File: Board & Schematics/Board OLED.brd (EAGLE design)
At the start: 25.4 x 25.4 mm, 23 parts

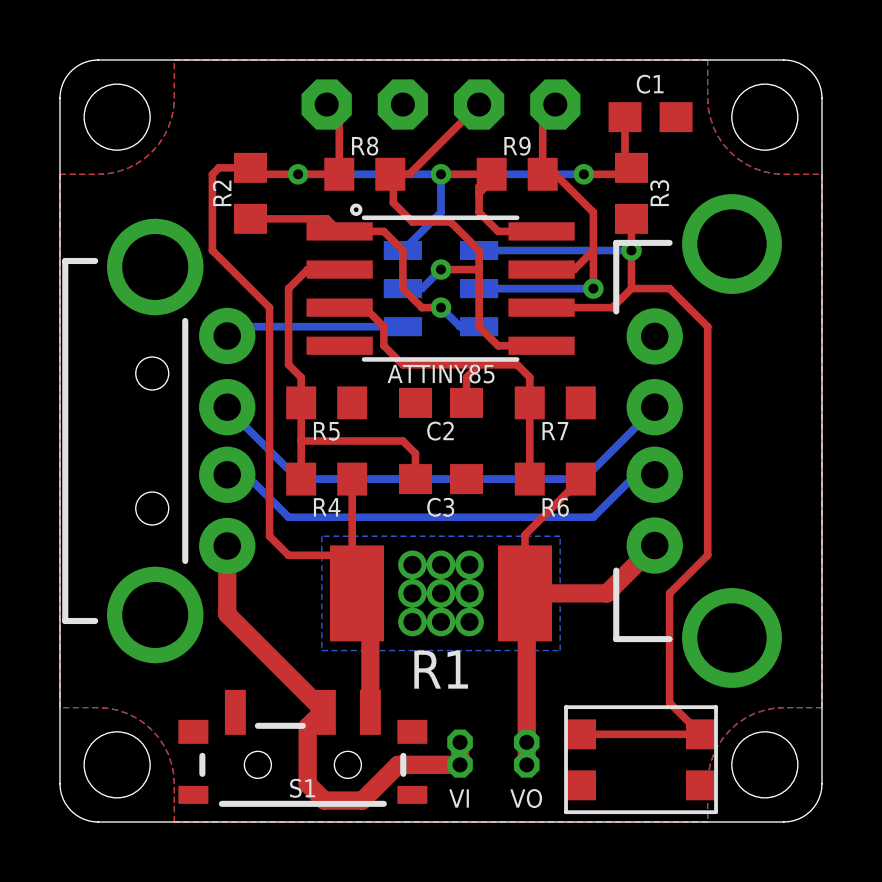
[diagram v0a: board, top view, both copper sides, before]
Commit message: removed cream from bottom ICSP Header
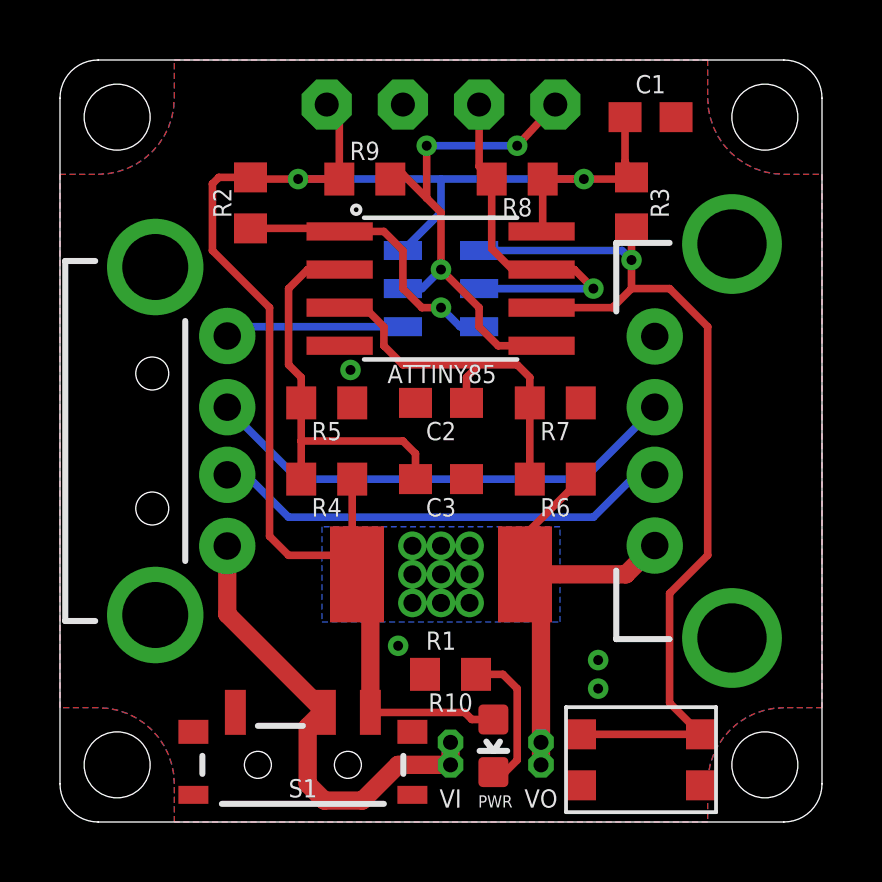
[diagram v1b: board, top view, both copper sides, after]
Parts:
- added PWR: (no value), SparkFun-LED:LED-0603
- added R10: 91Ω, rcl:R0603
- U$3: device OwnStuff:LOGO-SILKSCREEN -> OwnStuff:LOGO-SILKSCREEEN-S
- U$4: device SparkFun-Aesthetics:OSHW-LOGO-M -> SparkFun-Aesthetics:OSHW-LOGO-S
- moved U$4 14.3 mm to (9.05, 12.9)
- moved R8 5.08 mm to (15.2, 21.4), turned to 0 degrees
- moved R9 5.08 mm to (10.2, 21.4)
- moved U$3 2.34 mm to (14.9, 12.5)
- moved R1 0.64 mm to (12.7, 8.26)
- moved VO 0.48 mm to (16.0, 1.91)
- moved VI 0.32 mm to (13.0, 1.91)
- moved R2 0.32 mm to (6.35, 20.6)
- moved R3 0.32 mm to (19.1, 20.6)
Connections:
- new net N$4: PWR.C, R10.2
- net +5V: now also PWR.A
- net GND: now also R10.1
- net MOSI: now also R9.1, U$2.SDA; no longer R8.1, U$2.SCL
- net SCK: now also R8.1, U$2.SCL; no longer R9.1, U$2.SDA
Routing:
- net N$4: track 0.00 -> 4.91 mm
- net +5V: track 53.9 -> 56.7 mm, vias 3 -> 2
- net MOSI: track 16.1 -> 17.1 mm, vias 1 -> 3
- net N$6: track 15.8 -> 16.6 mm
- net GND: vias 0 -> 4

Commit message: added soldermask from vias
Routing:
- net GND: vias 4 -> 5

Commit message: fixed silkscreen and schematic designator for new, smaller shunt
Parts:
- R1: value 1Ω -> 0.1Ω
- moved R3 0.32 mm to (19.1, 21.0)
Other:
- board text added: "Shunt: 0.1Ω VI-VO=I[A]/10"
- board text removed: "Shunt: 1Ω VI-VO=I[A]"

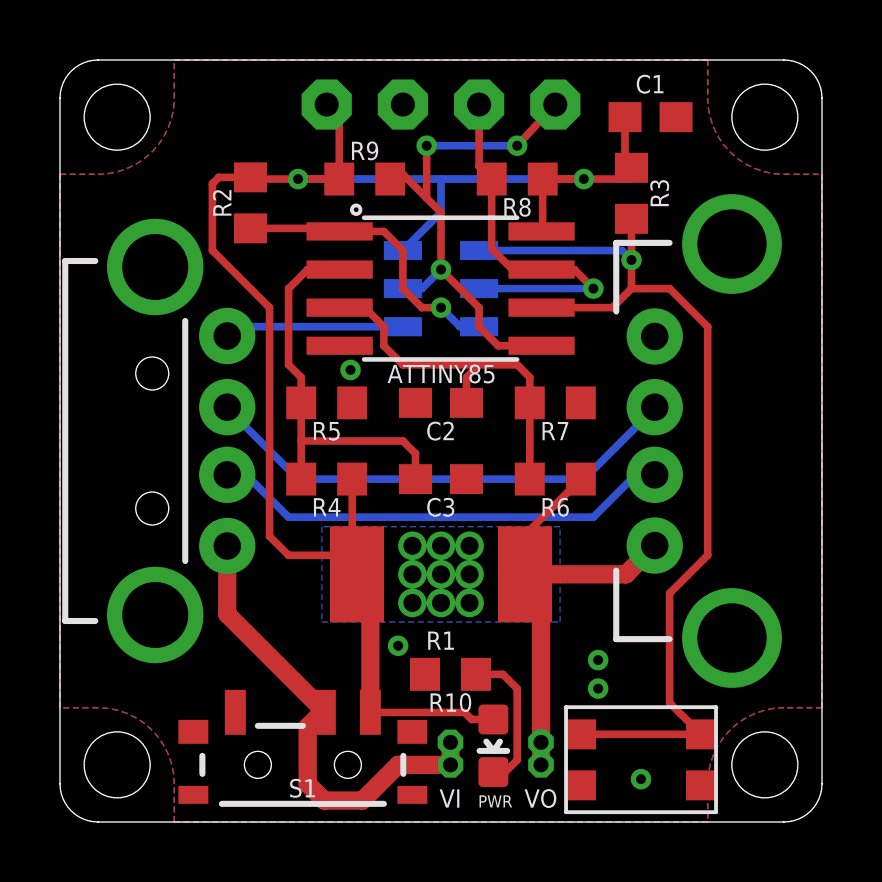
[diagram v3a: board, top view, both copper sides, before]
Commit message: remove attenuation from OLED variant
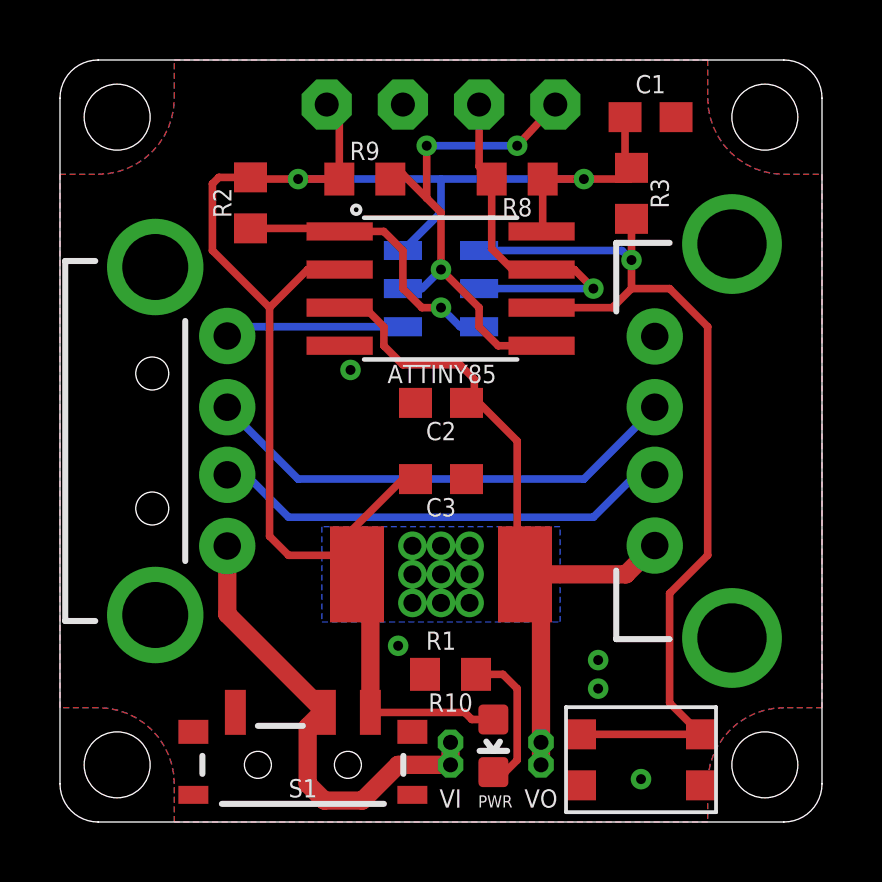
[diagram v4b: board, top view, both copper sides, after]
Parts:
- removed R4, R6: 10kΩ, rcl:R0603
- removed R5, R7: 2kΩ, rcl:R0603
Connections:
- removed net N$6: OUTPUT.VBUS, R1.2, R6.2, VO.P$1, VO.P$2
- removed net VSENSE: ATTINY85.2, C3.1, R4.1, R5.2
- net +5V: now also ATTINY85.2, C3.1; no longer R4.2
- net GND: no longer R5.1, R7.1
- net ISENSE: now also OUTPUT.VBUS, R1.2, VO.P$1, VO.P$2; no longer R6.1, R7.2
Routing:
- net N$6: track 16.6 -> 0.00 mm
- net ISENSE: track 12.5 -> 26.2 mm
- net VSENSE: track 13.3 -> 0.00 mm
- net +5V: track 56.7 -> 60.4 mm
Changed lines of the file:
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@@
 </element>
 <element name="U$1" library="OwnStuff" package="ICSP-SMD" value="ICSPSMD" x="12.7" y="17.78" rot="MR0"/>
-<element name="R4" library="rcl" package="R0603" value="10kΩ" x="8.89" y="11.43" smashed="yes">
-<attribute name="NAME" x="8.89" y="10.795" size="0.6096" layer="25" align="top-center"/>
-<attribute name="VALUE" x="8.255" y="9.525" size="1.27" layer="27"/>
-</element>
-<element name="R5" library="rcl" package="R0603" value="2kΩ" x="8.89" y="13.97" smashed="yes" rot="R180">
-<attribute name="NAME" x="8.89" y="13.335" size="0.6096" layer="25" rot="R180" align="bottom-center"/>
-<attribute name="VALUE" x="9.525" y="15.875" size="1.27" layer="27" rot="R180"/>
-</element>
-<element name="R6" library="rcl" package="R0603" value="10kΩ" x="16.51" y="11.43" smashed="yes">
-<attribute name="NAME" x="16.51" y="10.795" size="0.6096" layer="25" align="top-center"/>
-<attribute name="VALUE" x="15.875" y="9.525" size="1.27" layer="27"/>
-</element>
-<element name="R7" library="rcl" package="R0603" value="2kΩ" x="16.51" y="13.97" smashed="yes" rot="R180">
-<attribute name="NAME" x="16.51" y="13.335" size="0.6096" layer="25" rot="R180" align="bottom-center"/>
-<attribute name="VALUE" x="17.145" y="15.875" size="1.27" layer="27" rot="R180"/>
-</element>
 <element name="S1" library="SparkFun-Electromechanical" package="SWITCH-SPST-SMD-A" value="" x="8.09625" y="1.905" smashed="yes" rot="R180">
 <attribute name="NAME" x="8.09625" y="1.42875" size="0.6096" layer="25" rot="R180" align="bottom-center"/>
@@
 <contactref element="U$2" pad="GND"/>
 <contactref element="U$1" pad="GND"/>
-<contactref element="R5" pad="1"/>
-<contactref element="R7" pad="1"/>
 <contactref element="C2" pad="2"/>
 <contactref element="C3" pad="2"/>
@@
 <contactref element="S1" pad="1"/>
 <contactref element="R1" pad="1"/>
-<contactref element="R4" pad="2"/>
 <wire x1="9.87" y1="7.59" x2="9.9" y2="8.255" width="0.4064" layer="1"/>
-<wire x1="9.9" y1="11.27" x2="9.74" y2="11.43" width="0.254" layer="1"/>
-<wire x1="9.74" y1="11.43" x2="9.74" y2="8.89" width="0.254" layer="1"/>
 <wire x1="9.74" y1="8.89" x2="9.74" y2="7.78" width="0.254" layer="1"/>
 <wire x1="9.74" y1="7.78" x2="9.9" y2="8.255" width="0.254" layer="1"/>
@@
 <wire x1="13.49375" y1="3.65125" x2="10.35" y2="3.65125" width="0.254" layer="1"/>
 <wire x1="10.35" y1="3.65125" x2="10.34625" y2="3.655" width="0.254" layer="1"/>
+<contactref element="C3" pad="1"/>
+<wire x1="9.74" y1="8.89" x2="9.74" y2="9.74" width="0.254" layer="1"/>
+<wire x1="9.74" y1="9.74" x2="11.43" y2="11.43" width="0.254" layer="1"/>
+<wire x1="11.43" y1="11.43" x2="11.85" y2="11.43" width="0.254" layer="1"/>
+<contactref element="ATTINY85" pad="2"/>
+<wire x1="9.3218" y1="18.415" x2="8.255" y2="18.415" width="0.254" layer="1"/>
+<wire x1="8.255" y1="18.415" x2="6.985" y2="17.145" width="0.254" layer="1"/>
 </signal>
 <signal name="RST">
@@
 <wire x1="11.43" y1="19.05" x2="10.795" y2="19.685" width="0.254" layer="1"/>
 <wire x1="10.795" y1="19.685" x2="9.3218" y2="19.685" width="0.254" layer="1"/>
-</signal>
-<signal name="N$6">
-<contactref element="R1" pad="2"/>
-<contactref element="OUTPUT" pad="VBUS"/>
-<contactref element="R6" pad="2"/>
-<wire x1="15.5" y1="8.255" x2="15.5" y2="9.57" width="0.254" layer="1"/>
-<wire x1="15.5" y1="9.57" x2="17.36" y2="11.43" width="0.254" layer="1"/>
-<contactref element="VO" pad="P$2"/>
-<contactref element="VO" pad="P$1"/>
-<wire x1="15.5" y1="8.255" x2="18.865" y2="8.255" width="0.6096" layer="1"/>
-<wire x1="15.24" y1="7.36" x2="15.5" y2="8.255" width="0.6096" layer="1"/>
-<wire x1="15.5575" y1="7.6775" x2="15.5" y2="8.255" width="0.6096" layer="1"/>
-<wire x1="16.03375" y1="1.905" x2="16.03375" y2="2.655" width="0.6096" layer="1"/>
-<wire x1="16.03375" y1="2.655" x2="16.03375" y2="7.08625" width="0.6096" layer="1"/>
-<wire x1="16.03375" y1="7.08625" x2="15.5" y2="8.255" width="0.6096" layer="1"/>
-<wire x1="18.865" y1="8.255" x2="19.825" y2="9.215" width="0.6096" layer="1"/>
 </signal>
 <signal name="MOSI">
@@
 <wire x1="18.415" y1="17.145" x2="19.05" y2="17.78" width="0.254" layer="1"/>
 </signal>
-<signal name="VSENSE">
-<contactref element="ATTINY85" pad="2"/>
-<contactref element="R4" pad="1"/>
-<contactref element="R5" pad="2"/>
-<contactref element="C3" pad="1"/>
-<wire x1="8.04" y1="13.97" x2="8.04" y2="14.82" width="0.254" layer="1"/>
-<wire x1="8.04" y1="14.82" x2="7.62" y2="15.24" width="0.254" layer="1"/>
-<wire x1="7.62" y1="15.24" x2="7.62" y2="17.78" width="0.254" layer="1"/>
-<wire x1="7.62" y1="17.78" x2="8.255" y2="18.415" width="0.254" layer="1"/>
-<wire x1="8.255" y1="18.415" x2="9.3218" y2="18.415" width="0.254" layer="1"/>
-<wire x1="8.04" y1="11.43" x2="8.04" y2="12.7" width="0.254" layer="1"/>
-<wire x1="8.04" y1="12.7" x2="8.04" y2="13.97" width="0.254" layer="1"/>
-<wire x1="11.85" y1="11.43" x2="11.85" y2="12.28" width="0.254" layer="1"/>
-<wire x1="11.85" y1="12.28" x2="11.43" y2="12.7" width="0.254" layer="1"/>
-<wire x1="11.43" y1="12.7" x2="8.04" y2="12.7" width="0.254" layer="1"/>
-</signal>
 <signal name="ISENSE">
-<contactref element="R6" pad="1"/>
-<contactref element="R7" pad="2"/>
 <contactref element="C2" pad="1"/>
 <contactref element="ATTINY85" pad="3"/>
 <wire x1="10.795" y1="16.51" x2="10.16" y2="17.145" width="0.254" layer="1"/>
 <wire x1="10.16" y1="17.145" x2="9.3218" y2="17.145" width="0.254" layer="1"/>
-<wire x1="15.66" y1="11.43" x2="15.66" y2="13.97" width="0.254" layer="1"/>
-<wire x1="15.66" y1="13.97" x2="15.66" y2="14.82" width="0.254" layer="1"/>
-<wire x1="15.66" y1="14.82" x2="15.24" y2="15.24" width="0.254" layer="1"/>
 <wire x1="10.795" y1="16.51" x2="10.795" y2="15.875" width="0.254" layer="1"/>
 <wire x1="10.795" y1="15.875" x2="11.43" y2="15.24" width="0.254" layer="1"/>
-<wire x1="11.43" y1="15.24" x2="13.97" y2="15.24" width="0.254" layer="1"/>
-<wire x1="13.97" y1="15.24" x2="15.24" y2="15.24" width="0.254" layer="1"/>
-<wire x1="13.55" y1="13.97" x2="13.55" y2="14.82" width="0.254" layer="1"/>
-<wire x1="13.55" y1="14.82" x2="13.97" y2="15.24" width="0.254" layer="1"/>
+<contactref element="R1" pad="2"/>
+<contactref element="OUTPUT" pad="VBUS"/>
+<contactref element="VO" pad="P$2"/>
+<contactref element="VO" pad="P$1"/>
+<wire x1="15.5" y1="8.255" x2="18.865" y2="8.255" width="0.6096" layer="1"/>
+<wire x1="15.24" y1="7.36" x2="15.5" y2="8.255" width="0.6096" layer="1"/>
+<wire x1="15.5575" y1="7.6775" x2="15.5" y2="8.255" width="0.6096" layer="1"/>
+<wire x1="16.03375" y1="1.905" x2="16.03375" y2="2.655" width="0.6096" layer="1"/>
+<wire x1="16.03375" y1="2.655" x2="16.03375" y2="7.08625" width="0.6096" layer="1"/>
+<wire x1="16.03375" y1="7.08625" x2="15.5" y2="8.255" width="0.6096" layer="1"/>
+<wire x1="18.865" y1="8.255" x2="19.825" y2="9.215" width="0.6096" layer="1"/>
+<wire x1="11.43" y1="15.24" x2="13.335" y2="15.24" width="0.254" layer="1"/>
+<wire x1="13.335" y1="15.24" x2="13.81125" y2="14.76375" width="0.254" layer="1"/>
+<wire x1="13.81125" y1="14.76375" x2="13.81125" y2="14.23125" width="0.254" layer="1"/>
+<wire x1="13.81125" y1="14.23125" x2="13.55" y2="13.97" width="0.254" layer="1"/>
+<wire x1="13.55" y1="13.97" x2="13.97" y2="13.97" width="0.254" layer="1"/>
+<wire x1="13.97" y1="13.97" x2="15.24" y2="12.7" width="0.254" layer="1"/>
+<wire x1="15.24" y1="12.7" x2="15.24" y2="8.515" width="0.254" layer="1"/>
+<wire x1="15.24" y1="8.515" x2="15.5" y2="8.255" width="0.254" layer="1"/>
 </signal>
 <signal name="N$3">

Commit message: switched differential measure polarity
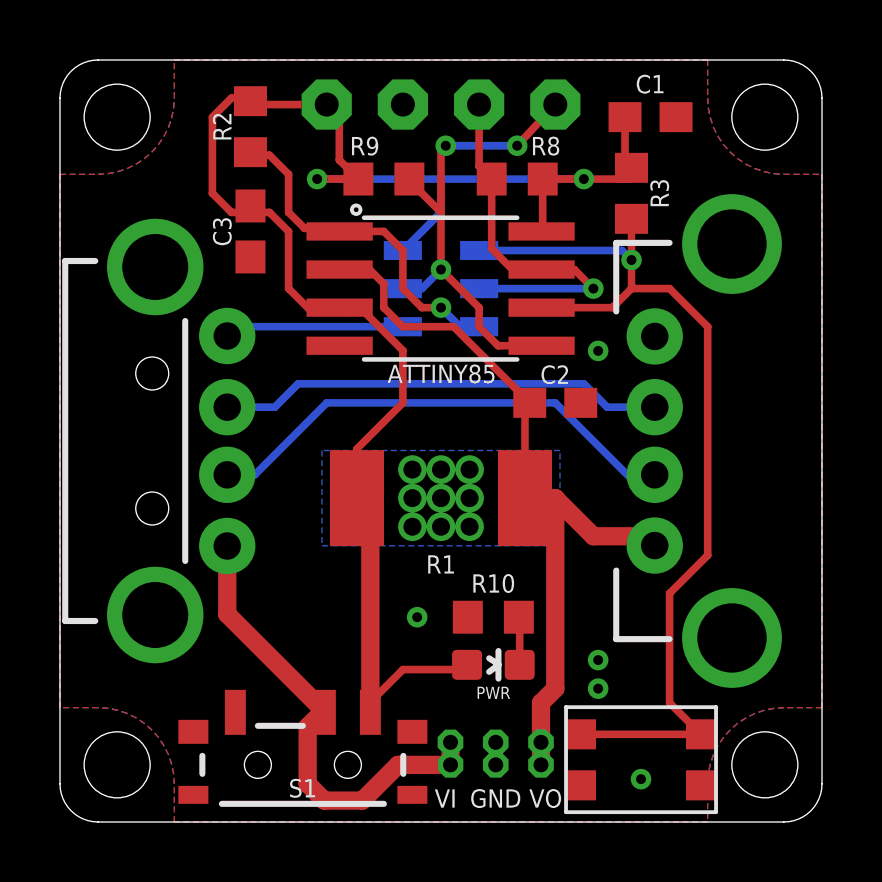
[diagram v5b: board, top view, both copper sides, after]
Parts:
- added GND: TESTPOINT0.5MM-DRILL-WIRE-LOOP, OwnStuff:TP-0.5MM-DUAL
- moved C3 10.4 mm to (6.35, 19.7), turned to 270 degrees
- moved U$4 6.05 mm to (8.57, 6.83)
- moved U$3 5.72 mm to (14.6, 6.83)
- moved C2 3.81 mm to (16.5, 14.0), turned to 0 degrees
- moved PWR 2.70 mm to (14.4, 5.24), turned to 270 degrees
- moved R1 2.54 mm to (12.7, 10.8)
- moved R2 2.54 mm to (6.35, 23.2)
- moved R10 2.38 mm to (14.4, 6.83)
- moved R9 0.63 mm to (10.8, 21.4)
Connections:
- net +5V: now also ATTINY85.3; no longer ATTINY85.2
- net GND: now also GND.P$1, GND.P$2
- net ISENSE: now also ATTINY85.2; no longer ATTINY85.3
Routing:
- net +5V: track 60.4 -> 56.7 mm
- net N$4: track 4.91 -> 1.60 mm
- net RST: track 9.72 -> 11.5 mm
- net N$1: track 16.4 -> 15.0 mm
- net N$2: track 15.4 -> 16.4 mm
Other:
- board text added: "GND"

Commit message: added attenuation resistor network to mode switch pin
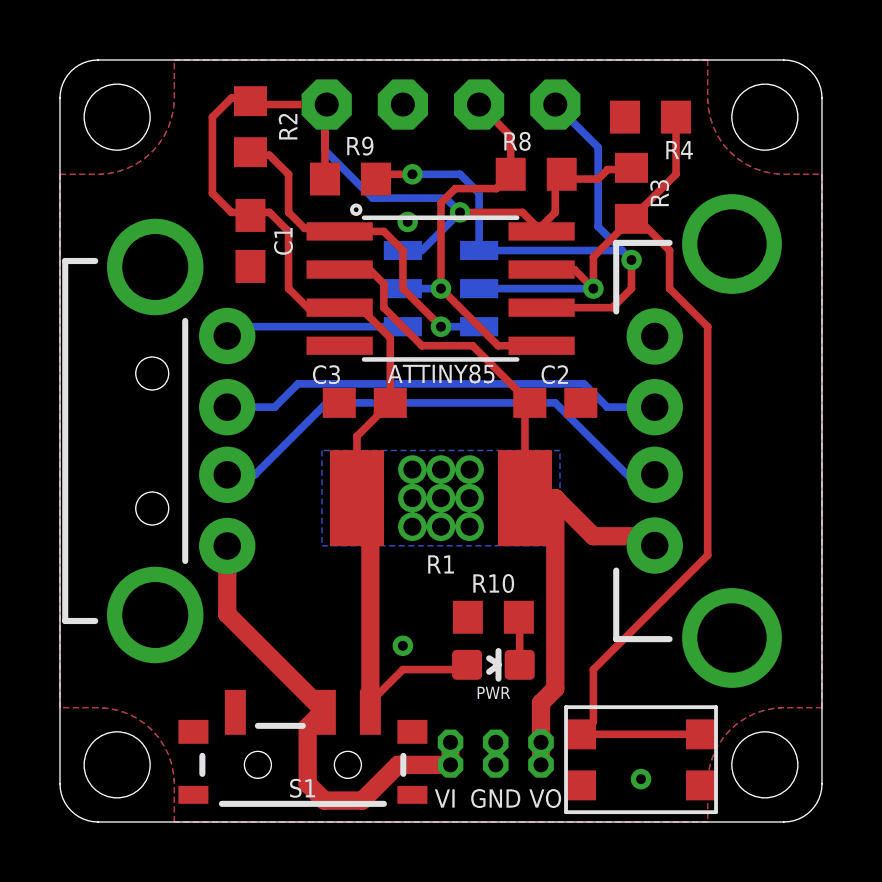
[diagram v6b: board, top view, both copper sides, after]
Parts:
- added R4: 2kΩ, rcl:R0603
- moved C1 14.0 mm to (6.35, 19.4), turned to 270 degrees
- moved C3 6.87 mm to (10.2, 14.0), turned to 180 degrees
- moved R9 1.11 mm to (9.68, 21.4)
- moved R8 0.65 mm to (15.9, 21.6)
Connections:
- net GND: now also R4.2
- net MISO: now also R9.1, U$2.SDA; no longer MODE.2, MODE.4, R3.1
- net MOSI: now also R8.1, U$2.SCL; no longer R9.1, U$2.SDA
- net SCK: now also MODE.2, MODE.4, R3.1, R4.1; no longer R8.1, U$2.SCL
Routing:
- net SCK: track 12.7 -> 37.1 mm
- net MISO: track 32.4 -> 20.9 mm, vias 1 -> 2
- net +5V: track 56.7 -> 52.8 mm, vias 2 -> 1
- net MOSI: track 16.8 -> 14.5 mm, vias 3 -> 1
- net GND: vias 5 -> 3
